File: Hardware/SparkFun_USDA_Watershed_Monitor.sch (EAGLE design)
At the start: 117 parts, among them J10 QWIIC_RIGHT_ANGLE, J12 3-PIN SMD, J3 QWIIC_RIGHT_ANGLE, J4 U.FL, J5 RJ45, J7 RJ45, J9 RJ45, Q1 20V/4.2A/52mΩ/1.4W, Q2 20V/0.2A/8MHz/1.2Ω/1Vth, Q3 20V/0.2A/8MHz/1.2Ω/1Vth, Q4 20V/0.2A/8MHz/1.2Ω/1Vth, Q5 20V/4.2A/52mΩ/1.4W, Q7 20V/4.2A/52mΩ/1.4W, U1 ESP-WROOM-3232D, U10 DNP, U11 RFM9XRFM95, U12 NAU7802SOIC, U2 AP3429A, U3 MCP73831, U5 BME680, U6 9DoF IMU, U7 1.8V/100mA, U8 CH340C, U9 DNP

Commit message: Add level shifter circuits for I2C sensors on VOUT
Sensors can get back powered through SDA and SCL pullups
Added MOSFET level shifter circuits to create new SDA/SCL_OUT nets with pullups to VOUT
Updated routing accordingly
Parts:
- added Q8, Q9: 20V/0.2A/8MHz/1.2Ω/1Vth, SparkFun-DiscreteSemi:MOSFET-NCH-RE1C002UNTCL
- added R29, R30: 2.2k, SparkFun-Resistors:2.2KOHM-0603-1/10W-1%
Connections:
- new net SCL_OUT: J10.4, Q3.D, Q9.S, R30.1, U10.SCL/SCK, U12.SCLK, U5.SCK/SCL, U9.SCL
- new net SDA_OUT: J10.3, Q2.D, Q8.S, R29.1, U10.SDA/SDI, U12.SDIO, U5.SDI/SDA, U9.SDA/SDI/SDO
- net SCL: now also Q9.D; no longer J10.4, Q3.D, U10.SCL/SCK, U12.SCLK, U5.SCK/SCL, U9.SCL
- net SDA: now also Q8.D; no longer J10.3, Q2.D, U10.SDA/SDI, U12.SDIO, U5.SDI/SDA, U9.SDA/SDI/SDO
- net VOUT: now also Q8.G, Q9.G, R29.2, R30.2
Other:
- note added: "1.8V Level Shifters"
- note added: "External I2C Level Shifters"
- note removed: "Level Shifting"
- moved on the sheet: BME_ADR, BOOT, C22, C23, D6, J10, J3, J4, Q7, R13, R26, R27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

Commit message: Design review updates
Bump version number to v10
Change BME_ADR from NO to NC
Add I2C addresses to silk
Remove hot warning from silk
Add better pin 1 indicator for BBME680
Add 100k pulldown on ESP_INT_COM net
Add measures for LEDs
Update Eagle libraries (adds tRestrict under U.FL connector)
Add axis labels for ICM's magnetometer, and gyro labels
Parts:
- added R28: 100k, SparkFun-Resistors:100KOHM-0603-1/10W-1%
- BME_ADR: value JUMPER-SMT_2_NO_SILK -> JUMPER-SMT_2_NC_TRACE_SILK; device SparkFun-Jumpers:JUMPER-SMT_2_NO_SILK -> SparkFun-Jumpers:JUMPER-SMT_2_NC_TRACE_SILK
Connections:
- net ESP_INT_COM: now also R28.1
- net GND: now also R28.2
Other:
- note added: "I2C default address: 0x76 Open BME_ADR: 0x77"
- note added: "v10"
- note removed: "I2C default address: 0x77 Close BME_ADR: 0x76"
- note removed: "v01"
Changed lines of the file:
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@@
 <part name="R13" library="SparkFun-Resistors" deviceset="100KOHM" device="-0603-1/10W-1%" value="100k"/>
 <part name="GND25" library="SparkFun-PowerSymbols" deviceset="GND" device=""/>
-<part name="BME_ADR" library="SparkFun-Jumpers" deviceset="JUMPER-SMT_2_NO" device="_SILK" package3d_urn="urn:adsk.eagle:package:39279/1"/>
+<part name="BME_ADR" library="SparkFun-Jumpers" deviceset="JUMPER-SMT_2_NC_TRACE" device="_SILK" package3d_urn="urn:adsk.eagle:package:39281/1"/>
 <part name="U6" library="SparkFun-Sensors" deviceset="ICM-20948" device="" value="9DoF IMU"/>
 <part name="U7" library="SparkFun-IC-Power" deviceset="V_REG_SP6214" device="-1.8V" value="1.8V/100mA"/>
@@
 <part name="SUPPLY53" library="SparkFun-PowerSymbols" deviceset="VOUT" device=""/>
 <part name="SUPPLY54" library="SparkFun-PowerSymbols" deviceset="VOUT" device=""/>
+<part name="R28" library="SparkFun-Resistors" deviceset="100KOHM" device="-0603-1/10W-1%" value="100k"/>
+<part name="GND62" library="SparkFun-PowerSymbols" deviceset="GND" device=""/>
 </parts>
 <sheets>
@@
 <plain>
 <text x="358.14" y="12.7" size="2.54" layer="94" font="vector" align="center">Dryw Wade</text>
-<text x="424.18" y="7.62" size="2.54" layer="94" font="vector" align="center">v01</text>
+<text x="645.16" y="83.82" size="2.54" layer="94" font="vector" align="center">v10</text>
 <text x="27.94" y="274.32" size="2.54" layer="94" font="vector" align="center">USB Connector</text>
 <text x="121.92" y="274.32" size="2.54" layer="94" font="vector" align="center">3V3 Regulator</text>
@@
 <text x="66.04" y="99.06" size="1.778" layer="97" font="vector" align="center">I2C default address: 0x6B
 Close ISM_ADR: 0x6A</text>
-<text x="220.98" y="106.68" size="1.778" layer="97" font="vector" align="center">I2C default address: 0x77
-Close BME_ADR: 0x76</text>
+<text x="220.98" y="106.68" size="1.778" layer="97" font="vector" align="center">I2C default address: 0x76
+Open BME_ADR: 0x77</text>
 <text x="195.58" y="30.48" size="1.778" layer="97" font="vector" align="center">I2C address: 0x2A</text>
 <text x="127" y="261.62" size="1.778" layer="97" font="vector" align="center">Max input: 5.5V</text>
@@
 <attribute name="VALUE" x="411.48" y="81.534" size="1.778" layer="96" font="vector" align="bottom-center"/>
 </instance>
+<instance part="R28" gate="G$1" x="337.82" y="104.14" smashed="yes">
+<attribute name="NAME" x="337.82" y="105.664" size="1.778" layer="95" font="vector" align="bottom-center"/>
+<attribute name="VALUE" x="337.82" y="102.616" size="1.778" layer="96" font="vector" align="top-center"/>
+</instance>
+<instance part="GND62" gate="1" x="345.44" y="99.06" smashed="yes">
+<attribute name="VALUE" x="345.44" y="98.806" size="1.778" layer="96" font="vector" align="top-center"/>
+</instance>
 </instances>
 <busses>
@@
 <wire x1="264.16" y1="71.12" x2="264.16" y2="76.2" width="0.1524" layer="91"/>
 <wire x1="264.16" y1="76.2" x2="266.7" y2="76.2" width="0.1524" layer="91"/>
+</segment>
+<segment>
+<pinref part="R28" gate="G$1" pin="2"/>
+<pinref part="GND62" gate="1" pin="GND"/>
+<wire x1="342.9" y1="104.14" x2="345.44" y2="104.14" width="0.1524" layer="91"/>
+<wire x1="345.44" y1="104.14" x2="345.44" y2="101.6" width="0.1524" layer="91"/>
 </segment>
 </net>
@@
 <label x="330.2" y="114.3" size="1.27" layer="95" font="vector" rot="R180" xref="yes"/>
 </segment>
-</net>
+<segment>
+<wire x1="332.74" y1="104.14" x2="330.2" y2="104.14" width="0.1524" layer="91"/>
+<label x="330.2" y="104.14" size="1.27" layer="95" font="vector" rot="R180" xref="yes"/>
+<pinref part="R28" gate="G$1" pin="1"/>
+</segment>
+</net>

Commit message: Design review updates
Add power control to CH340 (required some components in top right corner to be rearranged)
Nudge fiducials and OSHW logo
Update GPS connector silk
Update RJ45 connector "A" pinout silk to have "VO" instead of "3V3"
Fix STAT LED measure
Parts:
- added Q10: 20V/4.2A/52mΩ/1.4W, SparkFun-DiscreteSemi:MOSFET_PCH-DMG2305UX-7
- added Q11: 20V/0.2A/8MHz/1.2Ω/1Vth, SparkFun-DiscreteSemi:MOSFET-NCH-RE1C002UNTCL
- added R31: 100k, SparkFun-Resistors:100KOHM-0603-1/10W-1%
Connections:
- new net N$31: Q10.G, Q11.D, R31.1
- new net N$32: C14.1, Q10.D, U8.VCC
- net 3.3V: now also Q10.S, R31.2; no longer C14.1, U8.VCC
- net 5V: now also Q11.G
- net GND: now also Q11.S
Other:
- moved on the sheet: BOOT, C14, C6, J6, R26, RESET, U8

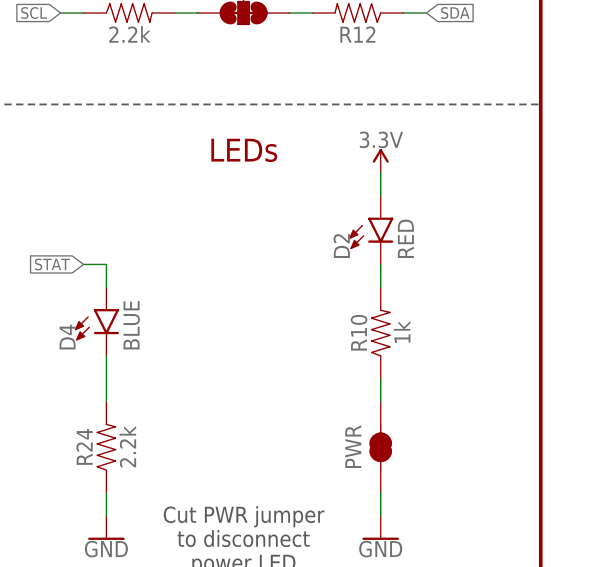
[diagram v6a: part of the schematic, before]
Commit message: Update power LED
Change to new SKU
Set as DNP
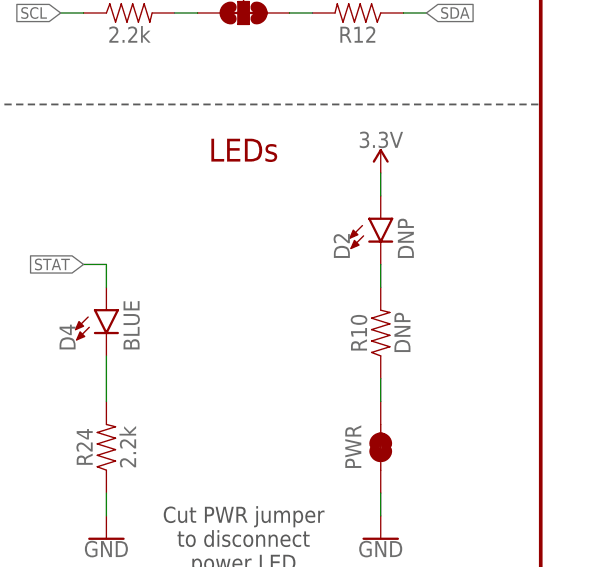
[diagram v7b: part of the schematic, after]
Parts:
- D2: value RED -> DNP; device SparkFun-LED:LED-RED0603 -> SparkFun-LED:LED-RED_0603-KB
- R10: value 1k -> DNP; device SparkFun-Resistors:1KOHM-0603-1/10W-1% -> SparkFun-Resistors:4.7KOHM-0603-1/10W-1%
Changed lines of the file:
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@@
 <part name="R7" library="SparkFun-Resistors" deviceset="4.7KOHM" device="-0603-1/10W-1%" value="4.7k"/>
 <part name="CHG" library="SparkFun-Jumpers" deviceset="JUMPER-SMT_2_NC_TRACE" device="_SILK" package3d_urn="urn:adsk.eagle:package:39281/1"/>
-<part name="D2" library="SparkFun-LED" deviceset="LED-RED" device="0603" value="RED"/>
+<part name="D2" library="SparkFun-LED" deviceset="LED-RED" device="_0603-KB" value="DNP">
+<attribute name="PROD_ID" value=""/>
+</part>
 <part name="D3" library="SparkFun-LED" deviceset="LED-YELLOW" device="0603" value="Yellow"/>
 <part name="GND11" library="SparkFun-PowerSymbols" deviceset="GND" device=""/>
@@
 <part name="GND15" library="SparkFun-PowerSymbols" deviceset="GND" device=""/>
 <part name="R8" library="SparkFun-Resistors" deviceset="2.2KOHM" device="-0603-1/10W-1%" value="2.2k"/>
-<part name="R10" library="SparkFun-Resistors" deviceset="1KOHM" device="-0603-1/10W-1%" value="1k"/>
+<part name="R10" library="SparkFun-Resistors" deviceset="4.7KOHM" device="-0603-1/10W-1%" value="DNP">
+<attribute name="PROD_ID" value=""/>
+</part>
 <part name="PWR" library="SparkFun-Jumpers" deviceset="JUMPER-SMT_2_NC_TRACE" device="_SILK" package3d_urn="urn:adsk.eagle:package:39281/1"/>
 <part name="GND16" library="SparkFun-PowerSymbols" deviceset="GND" device=""/>

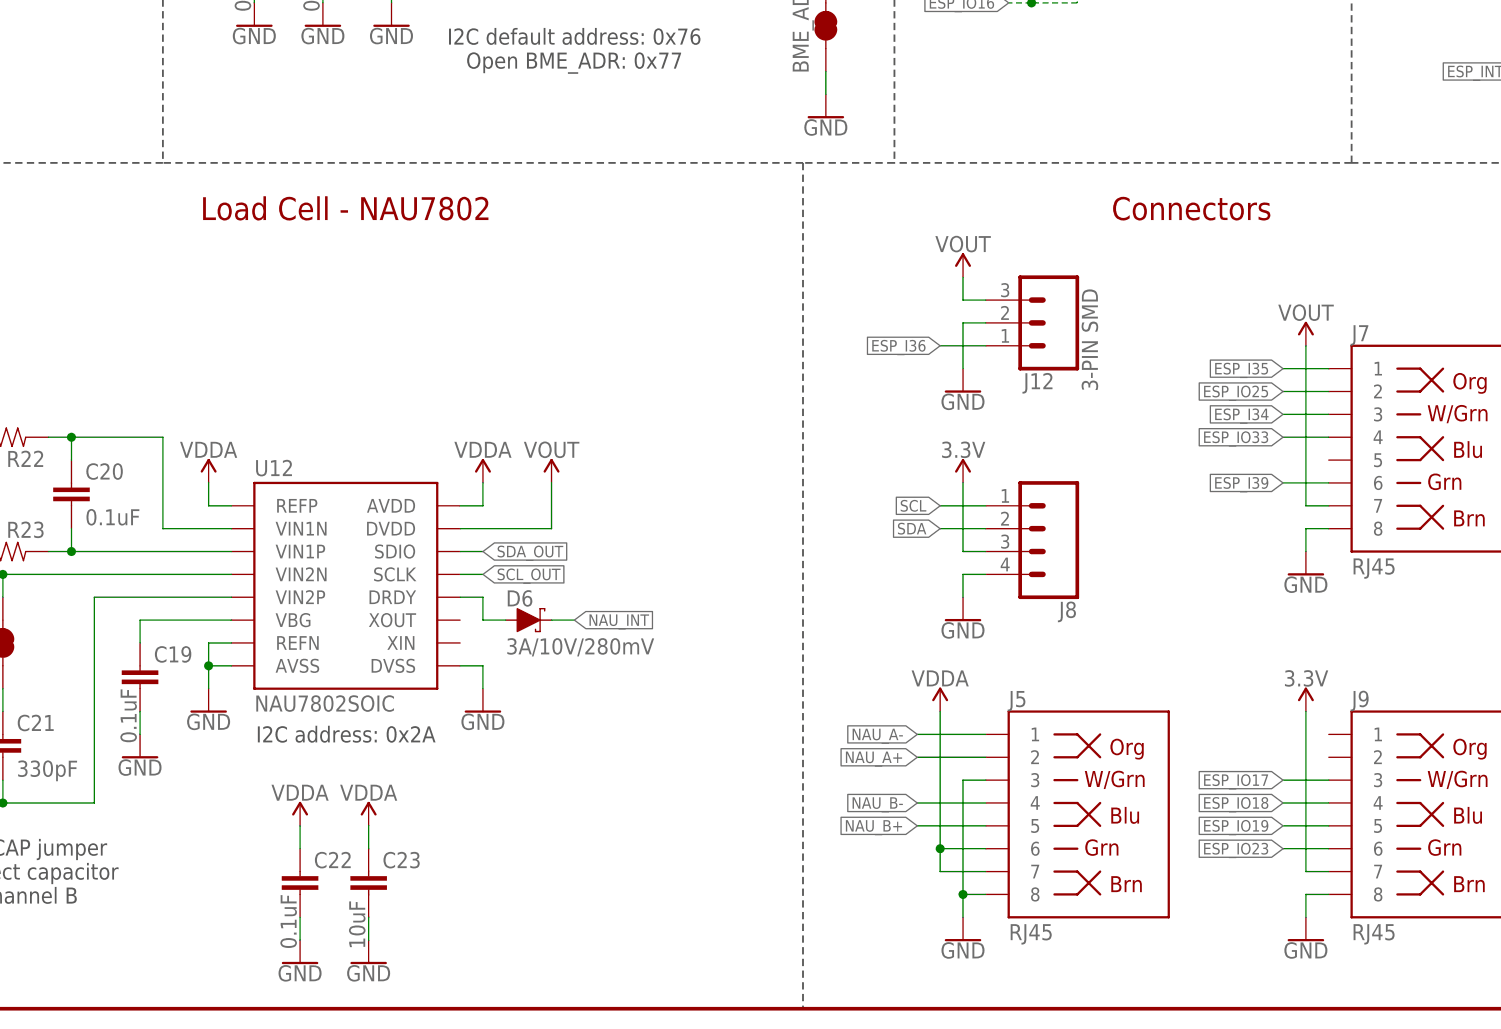
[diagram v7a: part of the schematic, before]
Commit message: Add 3V3 and VOUT to both RJ45 GPIO connectors
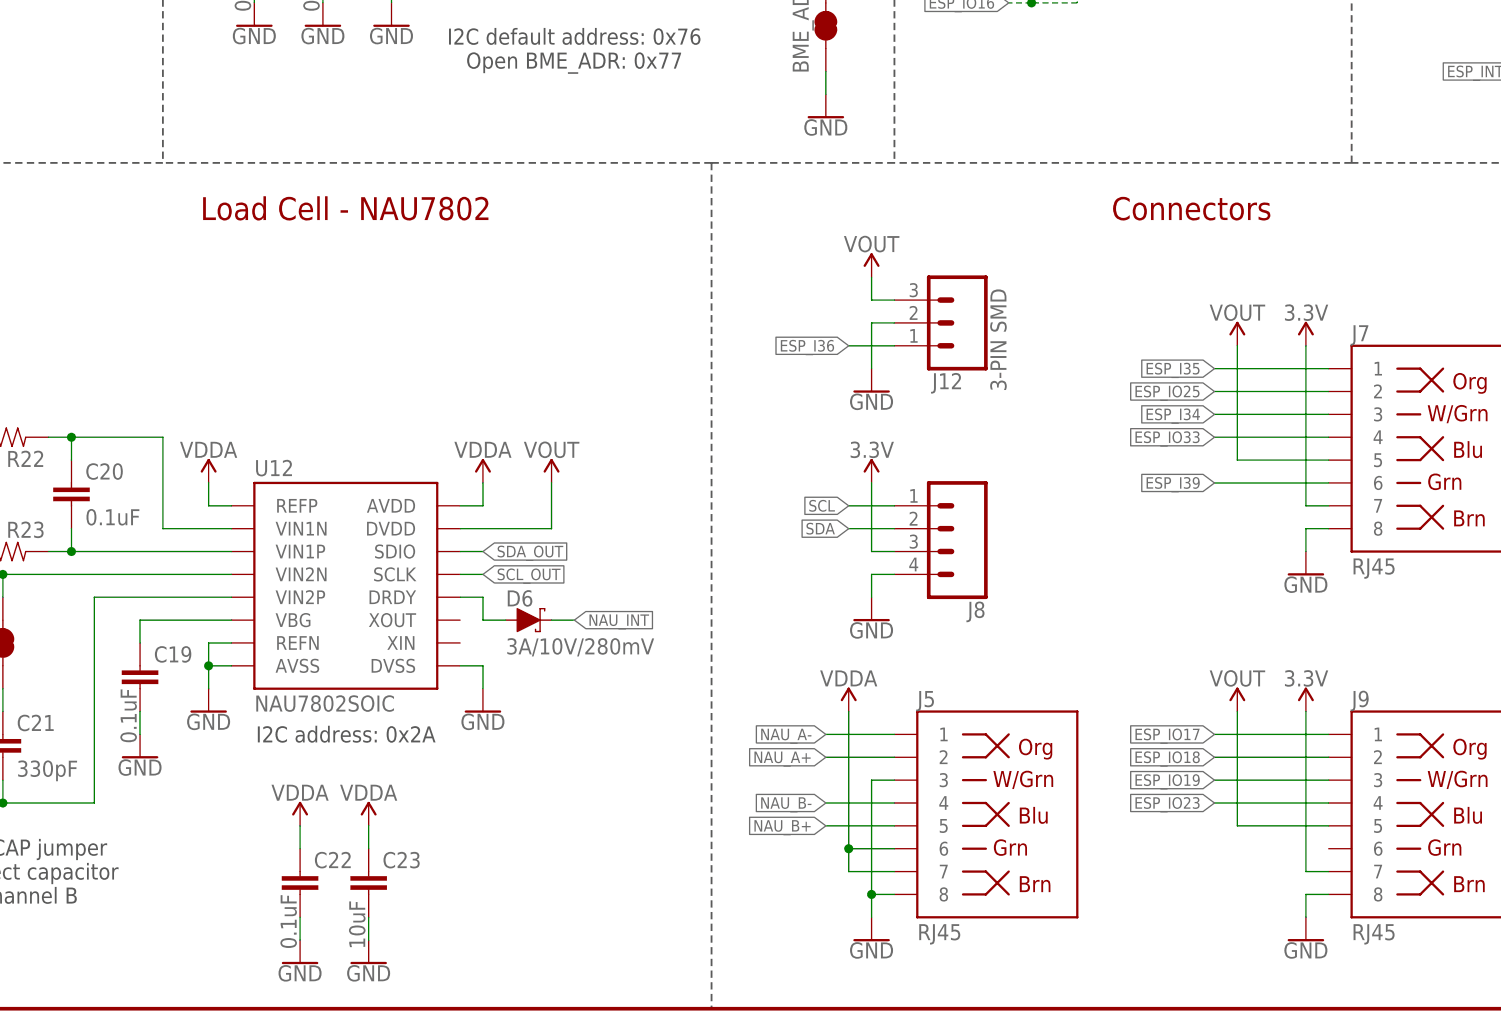
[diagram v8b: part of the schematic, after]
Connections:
- net 3.3V: now also J7.7
- net ESP_IO17: now also J9.1; no longer J9.3
- net ESP_IO18: now also J9.2; no longer J9.4
- net ESP_IO19: now also J9.3; no longer J9.5
- net ESP_IO23: now also J9.4; no longer J9.6
- net VOUT: now also J7.5, J9.5; no longer J7.7
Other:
- moved on the sheet: J12, J5, J8
